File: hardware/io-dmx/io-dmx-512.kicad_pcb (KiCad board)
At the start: 2 copper layers, 60 x 60 mm, 28 parts, among them J1 IO EXTENSION, J2 NC3FAH/NC5FAH, J3 NC3MAH/NC5MAH, U1 NMA0505SC, U2 6N137, U3 6N137, U4 6N137, U5 MAX3485CPA+

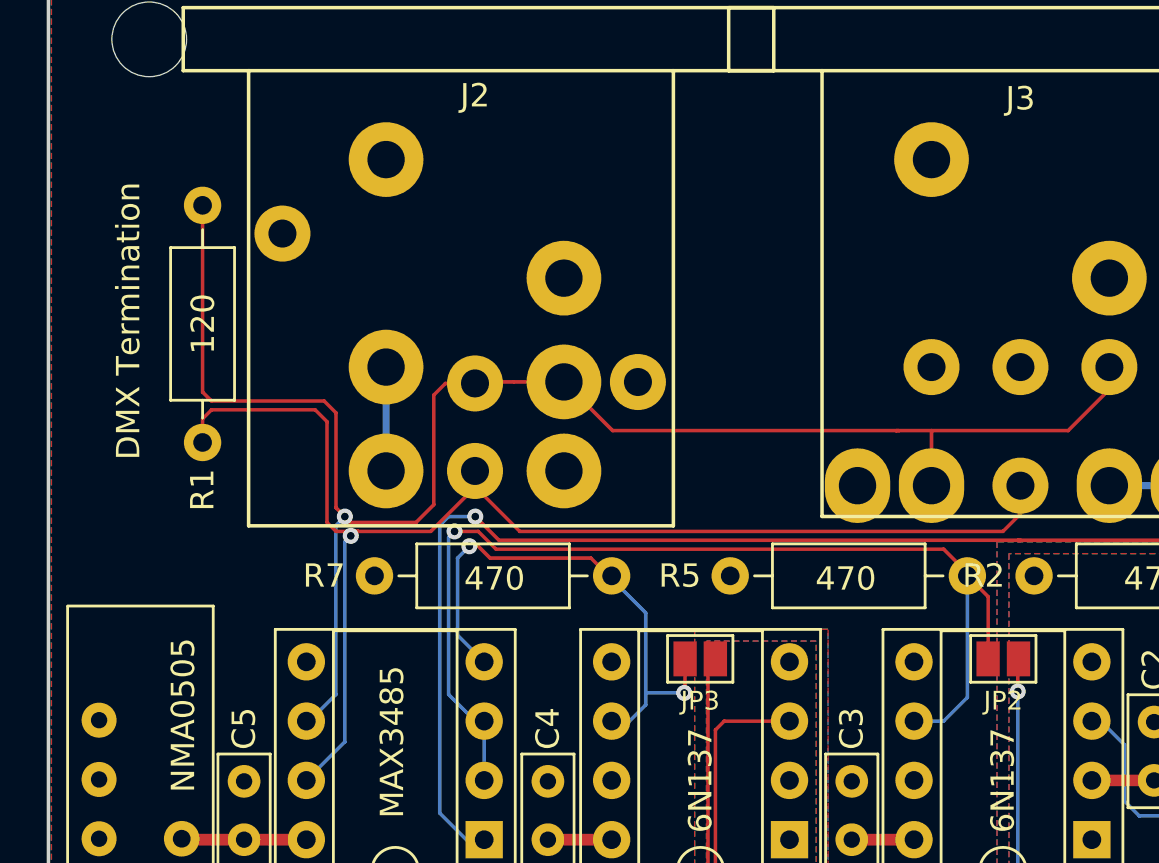
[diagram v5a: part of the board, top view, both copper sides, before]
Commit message: Tweaks boards based on construction notes
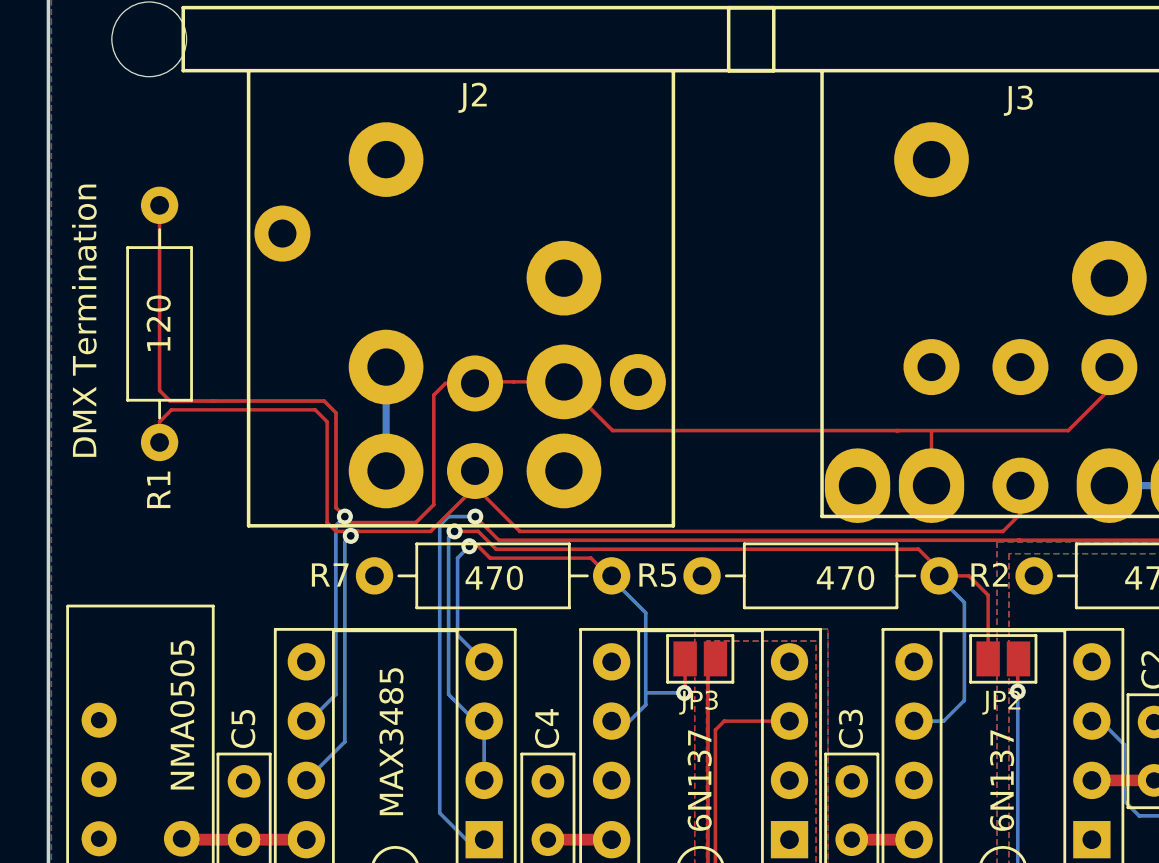
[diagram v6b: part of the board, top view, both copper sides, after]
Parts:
- moved R1 1.84 mm to (119.2, 71.9)
- moved R5 1.21 mm to (152.6, 87.8)
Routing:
- net Net-(J2-Pad2A): track 73.5 -> 75.5 mm
- net Net-(J2-Pad3): track 57.0 -> 58.8 mm
- net Net-(JP2-Pad2): track 46.3 -> 46.8 mm
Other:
- board text added: "DMX-IO1, Rev 1.5 Crazy Giraffe Software"
- board text removed: "DMX-IO1, Rev 1.4 Crazy Giraffe Software"
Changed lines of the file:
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@@
     (thickness 1.6)
     (drawings 28)
-    (tracks 195)
+    (tracks 200)
     (zones 0)
     (modules 28)
@@
   (title_block
     (title "DMX Demonstrator - DMX-512 IO Module (DMX-IO1)")
-    (date 2023-10-28)
-    (rev 1.4)
+    (date 2023-12-19)
+    (rev 1.5)
     (company "Crazy Giraffe Software")
     (comment 2 "Designed by: SparkyBobo")
@@
   )
   (module Resistor_THT:R_Axial_DIN0207_L6.3mm_D2.5mm_P10.16mm_Horizontal (layer F.Cu)
-    (at 121.031 71.882 270)
+    (at 119.1895 71.882 270)
     (descr "Resistor, Axial_DIN0207 series, Axial, Horizontal, pin pitch=10.16mm, 0.25W = 1/4W, length*diameter=6.3*2.5mm^2, http://cdn-reichelt.de/documents/datenblatt/B400/1_4W%23YAG.pdf")
     (tags "Resistor Axial_DIN0207 series Axial Horizontal pin pitch 10.16mm 0.25W = 1/4W length 6.3mm diameter 2.5mm")
@@
     (descr "Resistor, Axial_DIN0207 series, Axial, Horizontal, pin pitch=10.16mm, 0.25W = 1/4W, length*diameter=6.3*2.5mm^2, http://cdn-reichelt.de/documents/datenblatt/B400/1_4W%23YAG.pdf")
     (tags "Resistor Axial_DIN0207 series Axial Horizontal pin pitch 10.16mm 0.25W = 1/4W length 6.3mm diameter 2.5mm")
-    (fp_text reference R2 (at -2.159 0) (layer F.SilkS)
+    (fp_text reference R2 (at -1.905 0) (layer F.SilkS)
       (effects (font (size 1 1) (thickness 0.15)))
     )
@@
   )
   (module Resistor_THT:R_Axial_DIN0207_L6.3mm_D2.5mm_P10.16mm_Horizontal (layer F.Cu)
-    (at 153.797 87.757 180)
+    (at 152.5905 87.757 180)
     (descr "Resistor, Axial_DIN0207 series, Axial, Horizontal, pin pitch=10.16mm, 0.25W = 1/4W, length*diameter=6.3*2.5mm^2, http://cdn-reichelt.de/documents/datenblatt/B400/1_4W%23YAG.pdf")
     (tags "Resistor Axial_DIN0207 series Axial Horizontal pin pitch 10.16mm 0.25W = 1/4W length 6.3mm diameter 2.5mm")
-    (fp_text reference R5 (at 12.319 0 180) (layer F.SilkS)
+    (fp_text reference R5 (at 12.065 0 180) (layer F.SilkS)
       (effects (font (size 1 1) (thickness 0.15)))
     )
@@
     (descr "Resistor, Axial_DIN0207 series, Axial, Horizontal, pin pitch=10.16mm, 0.25W = 1/4W, length*diameter=6.3*2.5mm^2, http://cdn-reichelt.de/documents/datenblatt/B400/1_4W%23YAG.pdf")
     (tags "Resistor Axial_DIN0207 series Axial Horizontal pin pitch 10.16mm 0.25W = 1/4W length 6.3mm diameter 2.5mm")
-    (fp_text reference R7 (at 12.319 0 180) (layer F.SilkS)
+    (fp_text reference R7 (at 12.065 0 180) (layer F.SilkS)
       (effects (font (size 1 1) (thickness 0.15)))
     )
@@
     (effects (font (size 1 1) (thickness 0.15)))
   )
-  (gr_text 120 (at 121.0564 76.962 90) (layer F.SilkS)
+  (gr_text 120 (at 119.1895 76.962 90) (layer F.SilkS)
     (effects (font (size 1 1) (thickness 0.15)))
   )
-  (gr_text "DMX Termination" (at 117.856 76.835 90) (layer F.SilkS)
+  (gr_text "DMX Termination" (at 116.0145 76.835 90) (layer F.SilkS)
     (effects (font (size 1 1) (thickness 0.15)))
   )
@@
   (gr_line (start 174.427 61.397) (end 174.427 119.761) (layer Edge.Cuts) (width 0.15))
   (gr_line (start 115.189 60.579) (end 173.609 60.579) (layer Edge.Cuts) (width 0.15))
-  (gr_text "DMX-IO1, Rev 1.4\nCrazy Giraffe Software" (at 144.399 117.221) (layer B.SilkS)
+  (gr_text "DMX-IO1, Rev 1.5\nCrazy Giraffe Software" (at 144.399 117.221) (layer B.SilkS)
     (effects (font (size 1 1) (thickness 0.15)) (justify mirror))
   )
@@
   (segment (start 126.746 80.772) (end 126.746 84.836) (width 0.1524) (layer F.Cu) (net 4))
   (segment (start 126.238 80.264) (end 126.746 80.772) (width 0.1524) (layer F.Cu) (net 4))
-  (segment (start 121.412 80.264) (end 126.238 80.264) (width 0.1524) (layer F.Cu) (net 4))
-  (segment (start 121.031 71.882) (end 121.031 79.883) (width 0.1524) (layer F.Cu) (net 4))
-  (segment (start 121.031 79.883) (end 121.412 80.264) (width 0.1524) (layer F.Cu) (net 4))
   (segment (start 159.880793 79.768207) (end 159.880793 78.81216) (width 0.1524) (layer F.Cu) (net 4))
   (segment (start 152.273 81.534) (end 158.115 81.534) (width 0.1524) (layer F.Cu) (net 4))
@@
   (segment (start 125.603 93.98) (end 126.746 92.837) (width 0.1524) (layer B.Cu) (net 4))
   (segment (start 126.746 92.837) (end 126.746 85.598) (width 0.1524) (layer B.Cu) (net 4))
+  (segment (start 121.412 80.264) (end 121.6025 80.264) (width 0.1524) (layer F.Cu) (net 4))
+  (segment (start 121.6025 80.264) (end 126.238 80.264) (width 0.1524) (layer F.Cu) (net 4))
+  (segment (start 119.634 80.264) (end 121.6025 80.264) (width 0.1524) (layer F.Cu) (net 4))
+  (segment (start 119.1895 71.882) (end 119.1895 79.8195) (width 0.1524) (layer F.Cu) (net 4))
+  (segment (start 119.1895 79.8195) (end 119.634 80.264) (width 0.1524) (layer F.Cu) (net 4))
   (segment (start 127.127 94.869) (end 125.476 96.52) (width 0.1524) (layer B.Cu) (net 5))
   (segment (start 156.070793 85.102207) (end 156.070793 83.89216) (width 0.1524) (layer F.Cu) (net 5))
@@
   (segment (start 132.702793 83.26216) (end 132.702793 83.934793) (width 0.1524) (layer F.Cu) (net 5))
   (segment (start 132.702793 83.934793) (end 134.62 85.852) (width 0.1524) (layer F.Cu) (net 5))
-  (segment (start 121.031 81.026) (end 121.031 82.042) (width 0.1524) (layer F.Cu) (net 5))
-  (segment (start 121.412 80.645) (end 121.031 81.026) (width 0.1524) (layer F.Cu) (net 5))
-  (segment (start 125.857 80.645) (end 121.412 80.645) (width 0.1524) (layer F.Cu) (net 5))
   (segment (start 132.702793 83.26216) (end 132.702793 83.959207) (width 0.1524) (layer F.Cu) (net 5))
-  (segment (start 126.746 85.852) (end 126.365 85.471) (width 0.1524) (layer F.Cu) (net 5))
-  (segment (start 126.365 85.471) (end 126.365 81.153) (width 0.1524) (layer F.Cu) (net 5))
   (segment (start 132.702793 83.959207) (end 130.81 85.852) (width 0.1524) (layer F.Cu) (net 5))
-  (segment (start 126.365 81.153) (end 125.857 80.645) (width 0.1524) (layer F.Cu) (net 5))
   (via (at 127.381 86.0425) (size 0.6858) (drill 0.3302) (layers F.Cu B.Cu) (net 5))
   (segment (start 127.127 94.869) (end 127.127 86.2965) (width 0.1524) (layer B.Cu) (net 5))
@@
   (segment (start 127.381 86.0425) (end 127.5715 85.852) (width 0.1524) (layer F.Cu) (net 5))
   (segment (start 130.81 85.852) (end 127.6985 85.852) (width 0.1524) (layer F.Cu) (net 5))
-  (segment (start 127.6985 85.852) (end 126.746 85.852) (width 0.1524) (layer F.Cu) (net 5))
+  (segment (start 126.746 85.852) (end 127.6985 85.852) (width 0.1524) (layer F.Cu) (net 5))
+  (segment (start 119.1895 81.153) (end 119.6975 80.645) (width 0.1524) (layer F.Cu) (net 5))
+  (segment (start 119.1895 82.042) (end 119.1895 81.153) (width 0.1524) (layer F.Cu) (net 5))
+  (segment (start 119.6975 80.645) (end 125.857 80.645) (width 0.1524) (layer F.Cu) (net 5))
+  (segment (start 125.857 80.645) (end 126.365 81.153) (width 0.1524) (layer F.Cu) (net 5))
+  (segment (start 126.365 81.153) (end 126.365 85.471) (width 0.1524) (layer F.Cu) (net 5))
+  (segment (start 126.365 85.471) (end 126.746 85.852) (width 0.1524) (layer F.Cu) (net 5))
   (segment (start 151.511 99.06) (end 148.844 99.06) (width 0.5) (layer F.Cu) (net 10))
   (segment (start 122.809 99.06) (end 125.476 99.06) (width 0.5) (layer F.Cu) (net 10))
@@
   (segment (start 140.0175 93.2815) (end 139.319 93.98) (width 0.1524) (layer B.Cu) (net 34))
   (segment (start 133.096 96.52) (end 133.096 93.98) (width 0.1524) (layer B.Cu) (net 35))
-  (segment (start 152.781 93.98) (end 151.511 93.98) (width 0.1524) (layer B.Cu) (net 35))
-  (segment (start 153.797 87.757) (end 153.797 92.964) (width 0.1524) (layer B.Cu) (net 35))
-  (segment (start 153.797 92.964) (end 152.781 93.98) (width 0.1524) (layer B.Cu) (net 35))
-  (segment (start 153.797 87.63) (end 153.797 87.757) (width 0.1524) (layer F.Cu) (net 35))
-  (segment (start 152.781 86.614) (end 153.797 87.63) (width 0.1524) (layer F.Cu) (net 35))
-  (segment (start 133.604 86.614) (end 152.781 86.614) (width 0.1524) (layer F.Cu) (net 35))
   (segment (start 132.842 85.852) (end 133.604 86.614) (width 0.1524) (layer F.Cu) (net 35))
   (segment (start 131.826 85.852) (end 131.572 86.106) (width 0.1524) (layer B.Cu) (net 35))
@@
   (segment (start 132.715 93.98) (end 133.096 93.98) (width 0.1524) (layer B.Cu) (net 35))
   (segment (start 131.826 85.852) (end 132.842 85.852) (width 0.1524) (layer F.Cu) (net 35))
-  (segment (start 154.686 88.646) (end 153.797 87.757) (width 0.1524) (layer F.Cu) (net 35))
-  (segment (start 154.686 91.313) (end 154.686 88.646) (width 0.1524) (layer F.Cu) (net 35))
+  (segment (start 152.5905 87.503) (end 151.7015 86.614) (width 0.1524) (layer F.Cu) (net 35))
+  (segment (start 152.5905 87.757) (end 152.5905 87.503) (width 0.1524) (layer F.Cu) (net 35))
+  (segment (start 133.604 86.614) (end 151.7015 86.614) (width 0.1524) (layer F.Cu) (net 35))
+  (segment (start 153.8605 87.757) (end 152.5905 87.757) (width 0.1524) (layer F.Cu) (net 35))
+  (segment (start 154.686 91.313) (end 154.686 88.5825) (width 0.1524) (layer F.Cu) (net 35))
+  (segment (start 154.686 88.5825) (end 153.8605 87.757) (width 0.1524) (layer F.Cu) (net 35))
+  (segment (start 152.781 93.98) (end 151.511 93.98) (width 0.1524) (layer B.Cu) (net 35))
+  (segment (start 153.67 93.091) (end 152.781 93.98) (width 0.1524) (layer B.Cu) (net 35))
+  (segment (start 153.67 88.9) (end 153.67 93.091) (width 0.1524) (layer B.Cu) (net 35))
+  (segment (start 152.5905 87.757) (end 152.5905 87.8205) (width 0.1524) (layer B.Cu) (net 35))
+  (segment (start 152.5905 87.8205) (end 153.67 88.9) (width 0.1524) (layer B.Cu) (net 35))
   (segment (start 132.334 99.06) (end 133.096 99.06) (width 0.1524) (layer B.Cu) (net 36))
   (segment (start 131.191 97.917) (end 132.334 99.06) (width 0.1524) (layer B.Cu) (net 36))

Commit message: Consolidate parts library. Rebrand.
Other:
- board text added: "DMX-IO1, Rev 1.5 Sparky Bobo Designs"
- board text removed: "DMX-IO1, Rev 1.5 Crazy Giraffe Software"

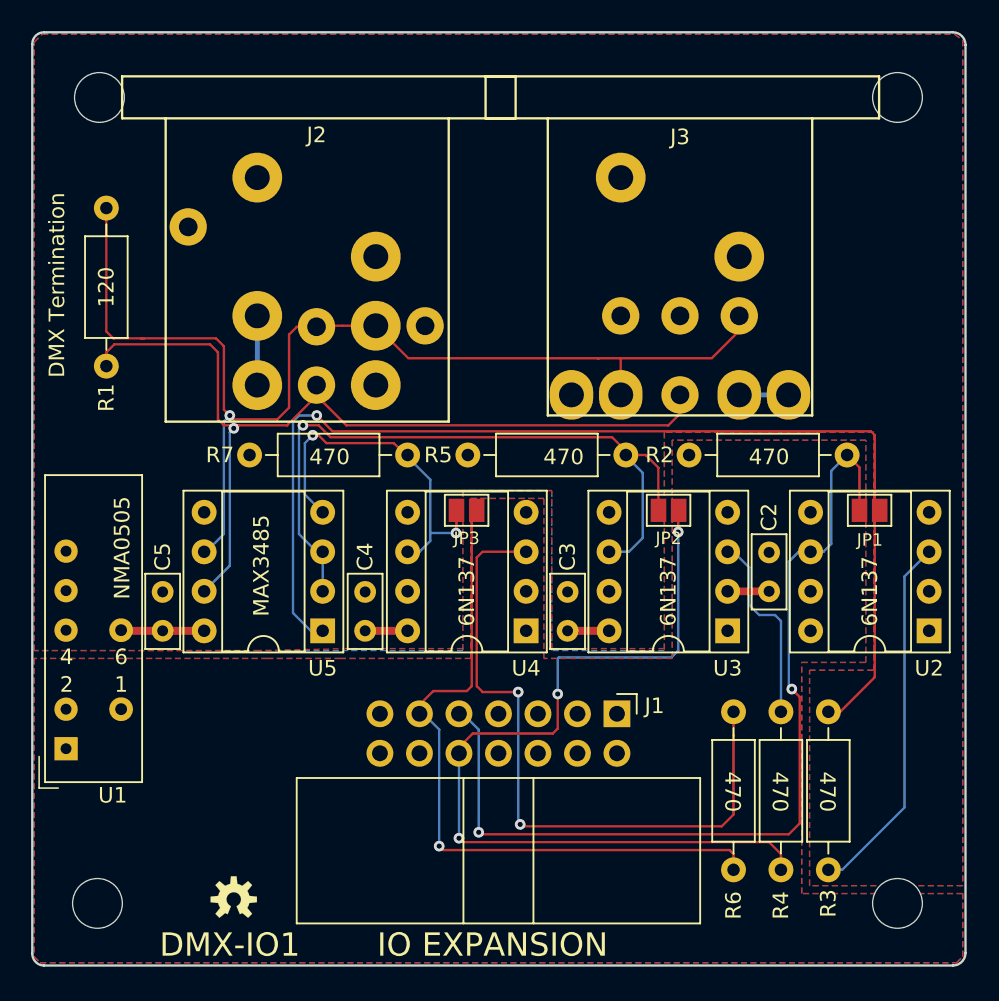
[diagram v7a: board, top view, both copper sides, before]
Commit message: - Added termination switch - Change to RFM-0505S - Change to MAX485E - Swap A and B on Max485 - Avoid split power planes under WH4 - Remove pads from XLR alignment pins - Update readme - Add IO1 parts to BOM generation.
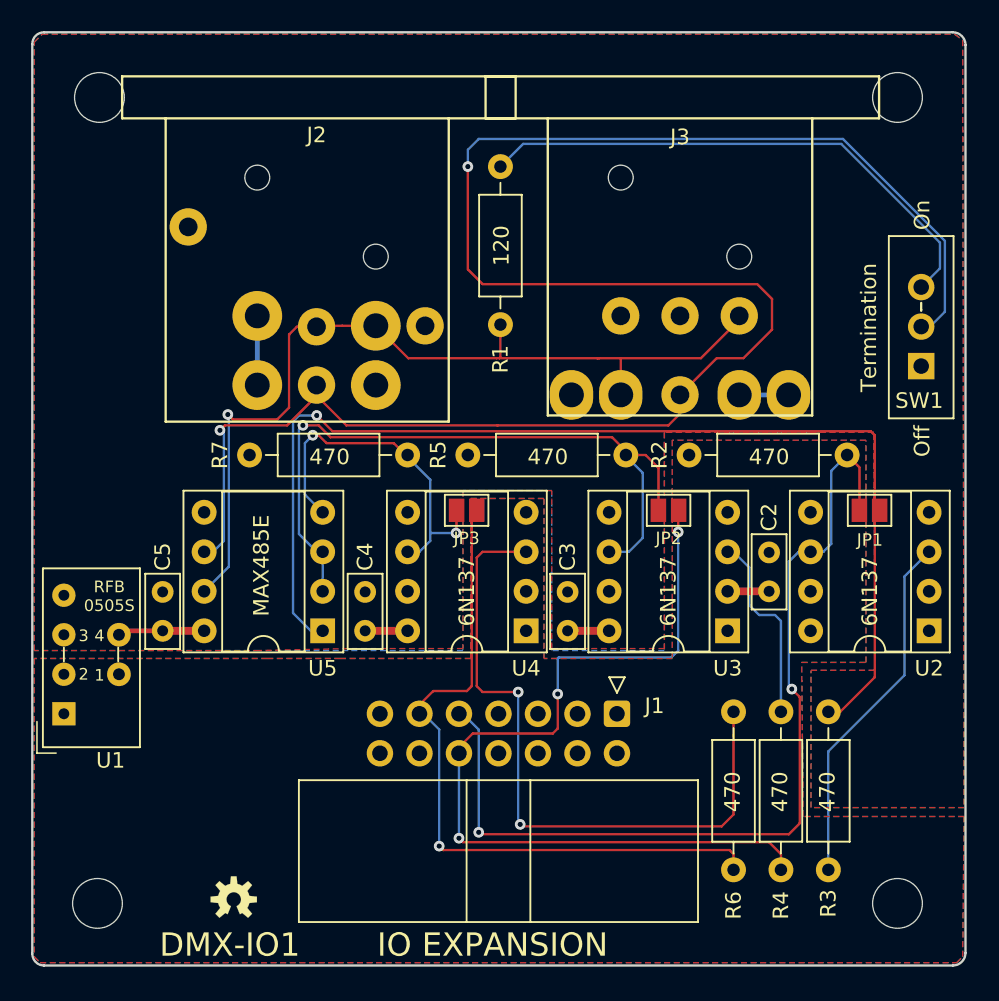
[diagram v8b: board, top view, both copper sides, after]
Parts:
- added SW1: TERM, footprints:ESWITCH_1218_SPDT, F.Cu at (171.6, 82.0)
- U1: value NMA0505SC -> RFM-0505S; footprint footprints:Converter_DCDC_muRata_NMAxxxxSC_THT_Bypass -> footprints:Converter_DCDC_Recom_RFM0505S_THT_Bypass
- U5: value MAX3485CPA+ -> MAX485
- moved R1 26.4 mm to (144.5, 79.4), turned to 90 degrees
- moved U1 2.25 mm to (116.5, 104.4)
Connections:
- R1 pad 2: Net-(J2-Pad3) -> Net-(R1-Pad2)
- U1 pad 4: GNDD -> VDD
- U5 pad 6: Net-(J2-Pad2A) -> Net-(J2-Pad3)
- U5 pad 7: Net-(J2-Pad3) -> Net-(J2-Pad2A)
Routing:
- net Net-(J2-Pad3): track 58.8 -> 120.9 mm, vias 1 -> 2
- net Net-(R1-Pad2): track 0.00 -> 34.8 mm
- net Net-(J2-Pad2A): track 75.5 -> 59.2 mm
- net Net-(R3-Pad2): track 23.7 -> 23.1 mm
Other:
- board text added: "3"
- board text added: "DMX-IO1, Rev 1.6 Sparky Bobo Designs"
- board text added: "MAX485E"
- board text added: "Off"
- board text added: "On"
- board text added: "RFB 0505S"
- board text added: "Termination"
- board text removed: "6"
- board text removed: "DMX Termination"
- board text removed: "DMX-IO1, Rev 1.5 Sparky Bobo Designs"
- board text removed: "MAX3485"
- board text removed: "NMA0505"
